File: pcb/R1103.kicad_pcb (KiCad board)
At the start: 2 copper layers, 26 x 63 mm, 6 parts, among them J1 COMPUTE_MOD_1, J2 SOCKET254P-02X20

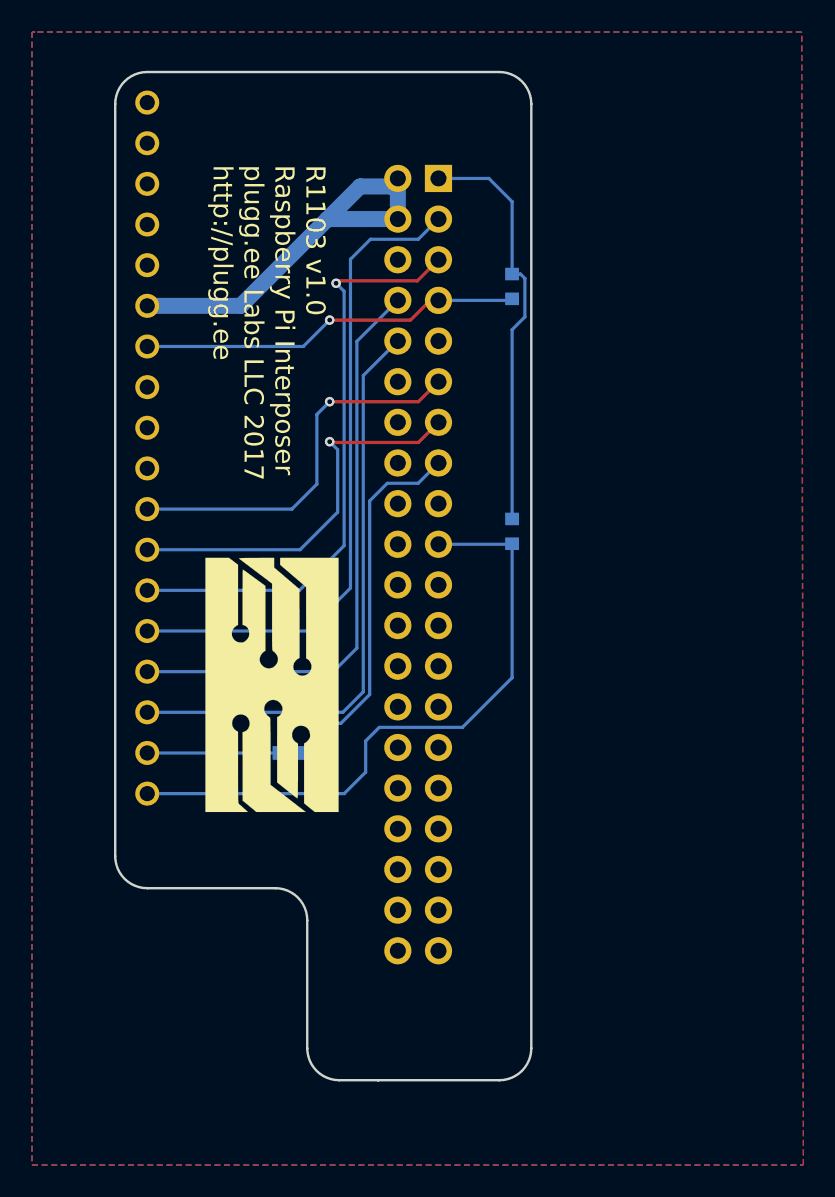
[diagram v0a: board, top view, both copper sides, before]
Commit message: adjusted layout to better fit RPi zero W
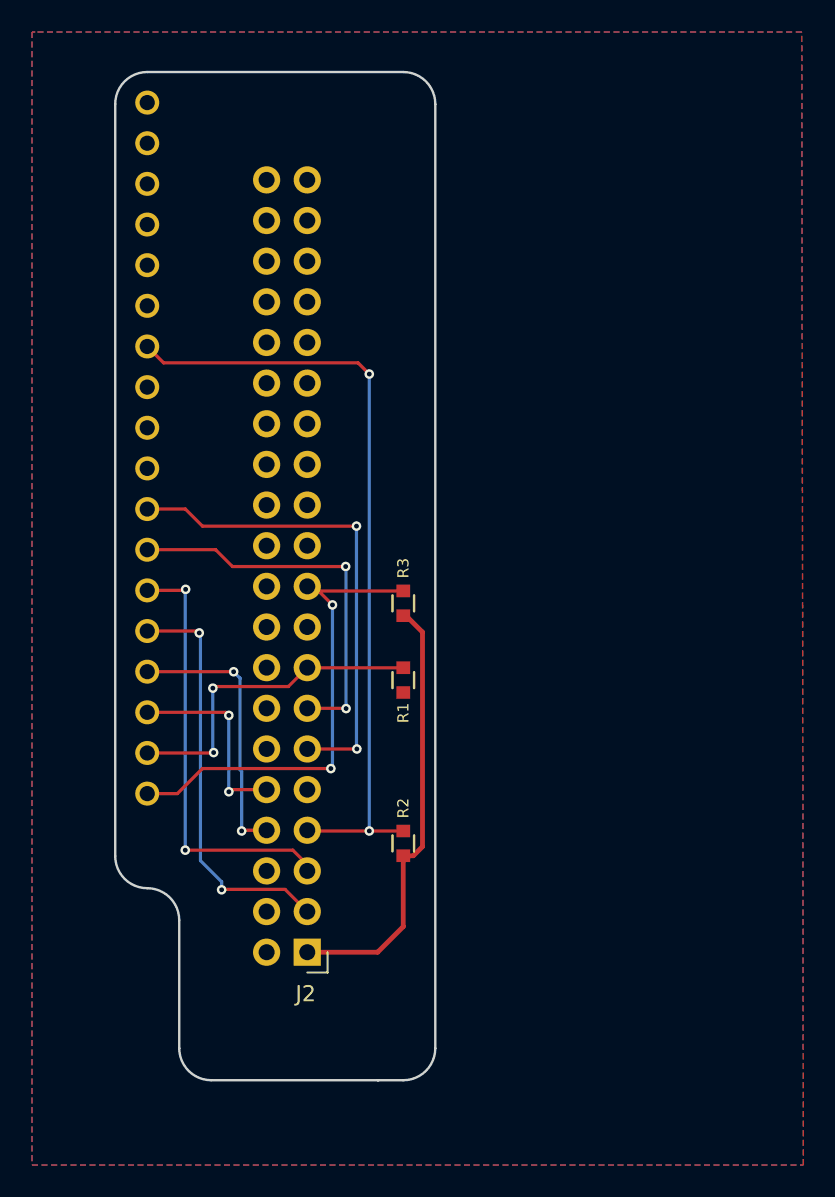
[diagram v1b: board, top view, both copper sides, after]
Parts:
- removed A1: ART, pluggee:pluggeeLabsIcon-16X8
- J2, R1, R2, R3: moved to F.Cu
- moved J2 49.0 mm to (138.0, 134.0)
- moved R2 35.5 mm to (144.0, 127.2), turned to 90 degrees
- moved R1 8.35 mm to (144.0, 117.0), turned to 270 degrees
- moved R3 8.15 mm to (144.0, 112.2), turned to 90 degrees
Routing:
- net +5V: track 25.9 -> 0.00 mm
- net /BTN: track 24.0 -> 49.2 mm, vias 1 -> 2
- net /SYSTXD0-RPiRX: track 36.8 -> 12.4 mm, vias 0 -> 2
- net /SYSRXD0-RPiTX: track 36.5 -> 17.1 mm, vias 0 -> 2
- net /SDA: track 40.9 -> 25.9 mm, vias 0 -> 2
- net /SWDCLK_BCM22: track 33.3 -> 20.6 mm, vias 0 -> 2
- net /SCK: track 37.1 -> 27.1 mm, vias 1 -> 2
- net /SWDIO_BCM10: track 39.9 -> 30.6 mm, vias 0 -> 2
- net /~RESET~_BCM17: track 24.0 -> 30.6 mm, vias 1 -> 2
- net +3.3VP: track 26.0 -> 27.6 mm
- net /~ISP~_BCM27: track 24.8 -> 24.2 mm, vias 1 -> 2
- added copper zone on B.Cu, net +5V
- removed copper zone on B.Cu, net GND
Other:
- board size 26 x 63 mm -> 20 x 63 mm
- board text added: "R1103 v1.2 Raspberry Pi Interposer http://plugg.ee"
- board text removed: "R1103 v1.0 Raspberry Pi Interposer plugg.ee Labs LLC 2017 http://plugg.ee"
